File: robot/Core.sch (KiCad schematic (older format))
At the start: 4 parts

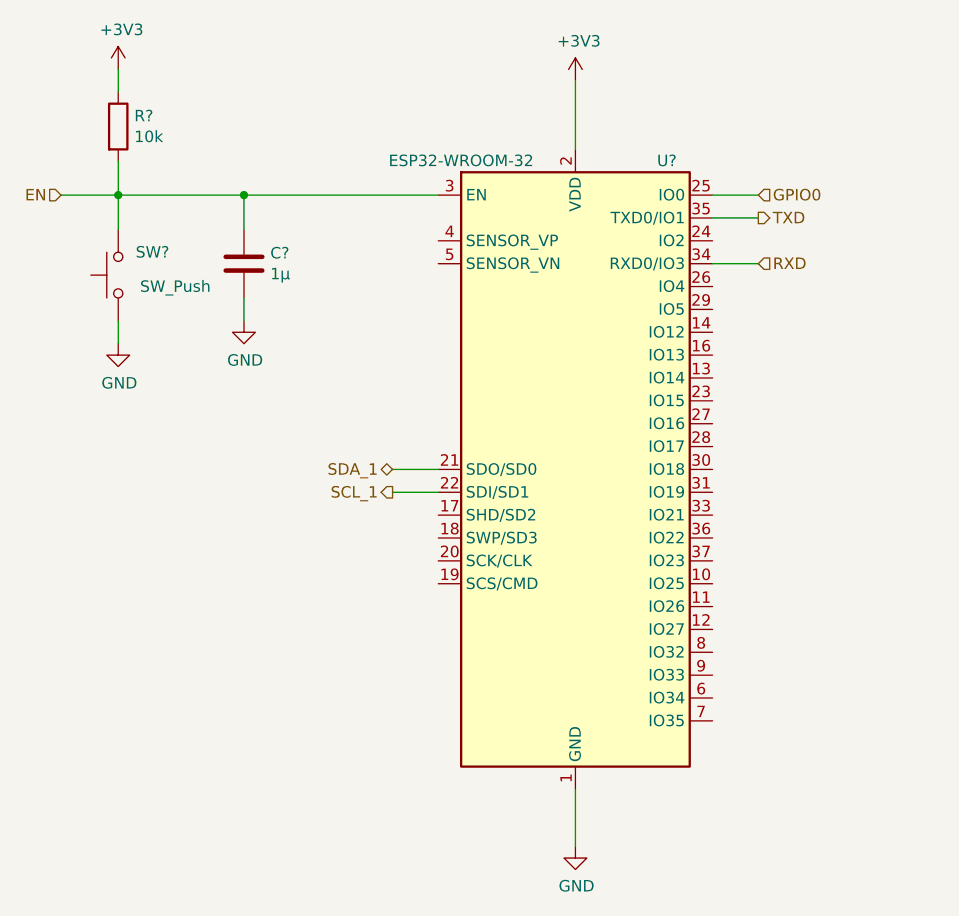
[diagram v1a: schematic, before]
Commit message: UI parts, (re)wiring remaining signals
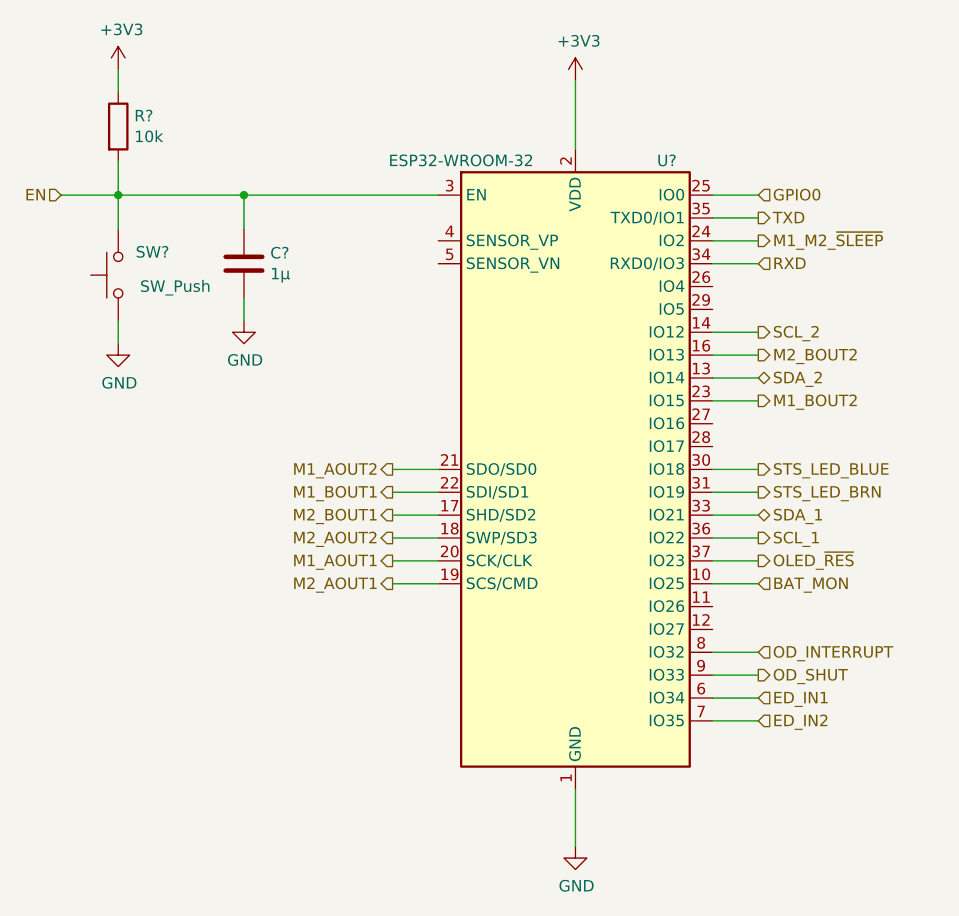
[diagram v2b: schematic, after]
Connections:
- net SCL_1: now also U?.36 (IO22); no longer U?.22 (SDI/SD1)
- net SDA_1: now also U?.33 (IO21); no longer U?.21 (SDO/SD0)
- net BAT_MON: now reaches U?.10 (IO25)
- net SDA_2: now reaches U?.13 (IO14)
- net SCL_2: now reaches U?.14 (IO12)
- net M2_BOUT2: now reaches U?.16 (IO13)
- net M2_BOUT1: now reaches U?.17 (SHD/SD2)
- net M2_AOUT2: now reaches U?.18 (SWP/SD3)
- net M2_AOUT1: now reaches U?.19 (SCS/CMD)
- net M1_AOUT1: now reaches U?.20 (SCK/CLK)
- net M1_BOUT2: now reaches U?.23 (IO15)
- net M1_M2_~SLEEP: now reaches U?.24 (IO2)
- net STS_LED_BLUE: now reaches U?.30 (IO18)
- net STS_LED_BRN: now reaches U?.31 (IO19)
- net OLED_~RES: now reaches U?.37 (IO23)
- net ED_IN1: now reaches U?.6 (IO34)
- net ED_IN2: now reaches U?.7 (IO35)
- net OD_INTERRUPT: now reaches U?.8 (IO32)
- net OD_SHUT: now reaches U?.9 (IO33)
- new net M1_AOUT2: U?.21 (SDO/SD0)
- new net M1_BOUT1: U?.22 (SDI/SD1)
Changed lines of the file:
@@
 $Descr A4 11693 8268
 encoding utf-8
-Sheet 3 7
+Sheet 8 8
 Title "Core"
 Date "2019-06-29"
@@
 Wire Wire Line
 	4200 2750 5050 2750
-Text HLabel 4850 3950 0    50   BiDi ~ 0
+Text HLabel 6450 4150 2    50   BiDi ~ 0
 SDA_1
+Text HLabel 6450 4250 2    50   Output ~ 0
+SCL_1
+Text HLabel 6450 3350 2    50   Output ~ 0
+SCL_2
+Text HLabel 6450 3550 2    50   BiDi ~ 0
+SDA_2
+Text HLabel 6450 3450 2    50   Output ~ 0
+M2_BOUT2
+Text HLabel 4850 4150 0    50   Output ~ 0
+M2_BOUT1
+Wire Wire Line
+	6250 3350 6450 3350
+Wire Wire Line
+	6250 3550 6450 3550
+Text HLabel 4850 4250 0    50   Output ~ 0
+M2_AOUT2
+Text HLabel 4850 4450 0    50   Output ~ 0
+M2_AOUT1
+Text HLabel 4850 4350 0    50   Output ~ 0
+M1_AOUT1
+Text HLabel 4850 3950 0    50   Output ~ 0
+M1_AOUT2
+Wire Wire Line
+	6250 4250 6450 4250
+Wire Wire Line
+	6450 4150 6250 4150
 Text HLabel 4850 4050 0    50   Output ~ 0
-SCL_1
+M1_BOUT1
+Text HLabel 6450 3650 2    50   Output ~ 0
+M1_BOUT2
+Text HLabel 6450 2950 2    50   Output ~ 0
+M1_M2_~SLEEP
 Wire Wire Line
 	4850 3950 5050 3950
 Wire Wire Line
 	4850 4050 5050 4050
+Wire Wire Line
+	4850 4150 5050 4150
+Wire Wire Line
+	4850 4250 5050 4250
+Wire Wire Line
+	4850 4350 5050 4350
+Wire Wire Line
+	4850 4450 5050 4450
+Wire Wire Line
+	6450 2950 6250 2950
+Wire Wire Line
+	6450 3450 6250 3450
+Wire Wire Line
+	6450 3650 6250 3650
+Text HLabel 6450 4950 2    50   Input ~ 0
+ED_IN1
+Text HLabel 6450 5050 2    50   Input ~ 0
+ED_IN2
+Wire Wire Line
+	6250 5050 6450 5050
+Wire Wire Line
+	6250 4950 6450 4950
+Text HLabel 6450 4450 2    50   Input ~ 0
+BAT_MON
+Text HLabel 6450 4750 2    50   Input ~ 0
+OD_INTERRUPT
+Text HLabel 6450 4850 2    50   Output ~ 0
+OD_SHUT
+Wire Wire Line
+	6250 4750 6450 4750
+Wire Wire Line
+	6250 4850 6450 4850
+Wire Wire Line
+	6250 4450 6450 4450
+Text HLabel 6450 3950 2    50   Output ~ 0
+STS_LED_BLUE
+Text HLabel 6450 4050 2    50   Output ~ 0
+STS_LED_BRN
+Wire Wire Line
+	6250 4050 6450 4050
+Wire Wire Line
+	6250 3950 6450 3950
+Text HLabel 6450 4350 2    50   Output ~ 0
+OLED_~RES
+Wire Wire Line
+	6250 4350 6450 4350
 $EndSCHEMATC

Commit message: DRC check fixes and small changes
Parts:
- gave numbers to parts that had none: 4
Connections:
- no-connect marks 0 -> 8
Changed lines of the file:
@@
 $EndDescr
 $Comp
-L RF_Module:ESP32-WROOM-32 U?
+L RF_Module:ESP32-WROOM-32 U10
 U 1 1 5D2E3B23
 P 5650 3950
-F 0 "U?" H 6050 5300 50  0000 C CNN
+F 0 "U10" H 6050 5300 50  0000 C CNN
 F 1 "ESP32-WROOM-32" H 5150 5300 50  0000 C CNN
 F 2 "RF_Module:ESP32-WROOM-32" H 5650 2450 50  0001 C CNN
@@
 	6250 2750 6450 2750
 $Comp
-L Device:C C?
+L Device:C C19
 U 1 1 5D6294B0
 P 4200 3050
-F 0 "C?" H 4315 3096 50  0000 L CNN
+F 0 "C19" H 4315 3096 50  0000 L CNN
 F 1 "1µ" H 4315 3005 50  0000 L CNN
 F 2 "" H 4238 2900 50  0001 C CNN
@@
 $EndComp
 $Comp
-L Switch:SW_Push SW?
+L Switch:SW_Push SW1
 U 1 1 5D62C889
 P 3650 3100
-F 0 "SW?" V 3750 2950 50  0000 C CNN
+F 0 "SW1" V 3750 2950 50  0000 C CNN
 F 1 "SW_Push" V 3600 2850 50  0000 C CNN
 F 2 "" H 3650 3300 50  0001 C CNN
@@
 $EndComp
 $Comp
-L Device:R R?
+L Device:R R18
 U 1 1 5D62DCB0
 P 3650 2450
-F 0 "R?" H 3720 2496 50  0000 L CNN
+F 0 "R18" H 3720 2496 50  0000 L CNN
 F 1 "10k" H 3720 2405 50  0000 L CNN
 F 2 "" V 3580 2450 50  0001 C CNN
@@
 Wire Wire Line
 	6250 4350 6450 4350
+NoConn ~ 6250 3150
+NoConn ~ 6250 3250
+NoConn ~ 6250 3750
+NoConn ~ 6250 3850
+NoConn ~ 6250 4550
+NoConn ~ 6250 4650
+NoConn ~ 5050 3050
+NoConn ~ 5050 2950
 $EndSCHEMATC

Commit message: Testpoints, switch, small changes
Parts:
- renumbered SW1 to SW2
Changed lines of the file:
@@
 $EndComp
 $Comp
-L power:+3V3 #PWR0128
+L power:+3V3 #PWR047
 U 1 1 5D2E60B8
 P 5650 2250
-F 0 "#PWR0128" H 5650 2100 50  0001 C CNN
+F 0 "#PWR047" H 5650 2100 50  0001 C CNN
 F 1 "+3V3" H 5665 2423 50  0000 C CNN
 F 2 "" H 5650 2250 50  0001 C CNN
@@
 	5650 2550 5650 2250
 $Comp
-L power:GND #PWR0129
+L power:GND #PWR050
 U 1 1 5D2E6C58
 P 5650 5600
-F 0 "#PWR0129" H 5650 5350 50  0001 C CNN
+F 0 "#PWR050" H 5650 5350 50  0001 C CNN
 F 1 "GND" H 5655 5427 50  0000 C CNN
 F 2 "" H 5650 5600 50  0001 C CNN
@@
 $EndComp
 $Comp
-L Switch:SW_Push SW1
+L Switch:SW_Push SW2
 U 1 1 5D62C889
 P 3650 3100
-F 0 "SW1" V 3750 2950 50  0000 C CNN
+F 0 "SW2" V 3750 2950 50  0000 C CNN
 F 1 "SW_Push" V 3600 2850 50  0000 C CNN
 F 2 "" H 3650 3300 50  0001 C CNN
@@
 $EndComp
 $Comp
-L power:+3V3 #PWR0130
+L power:+3V3 #PWR046
 U 1 1 5D62E308
 P 3650 2200
-F 0 "#PWR0130" H 3650 2050 50  0001 C CNN
+F 0 "#PWR046" H 3650 2050 50  0001 C CNN
 F 1 "+3V3" H 3665 2373 50  0000 C CNN
 F 2 "" H 3650 2200 50  0001 C CNN
@@
 $EndComp
 $Comp
-L power:GND #PWR0131
+L power:GND #PWR049
 U 1 1 5D62E7C3
 P 3650 3400
-F 0 "#PWR0131" H 3650 3150 50  0001 C CNN
+F 0 "#PWR049" H 3650 3150 50  0001 C CNN
 F 1 "GND" H 3655 3227 50  0000 C CNN
 F 2 "" H 3650 3400 50  0001 C CNN
@@
 $EndComp
 $Comp
-L power:GND #PWR0132
+L power:GND #PWR048
 U 1 1 5D62EDF6
 P 4200 3300
-F 0 "#PWR0132" H 4200 3050 50  0001 C CNN
+F 0 "#PWR048" H 4200 3050 50  0001 C CNN
 F 1 "GND" H 4205 3127 50  0000 C CNN
 F 2 "" H 4200 3300 50  0001 C CNN
